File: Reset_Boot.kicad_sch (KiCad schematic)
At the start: 23 parts, among them J301 Micro_SD_Card, J302 Molex PicoBlade 4-pin, Q301 BSS138, SW301 KMR2, SW302 KMR2, U301 SSM2518CPZ

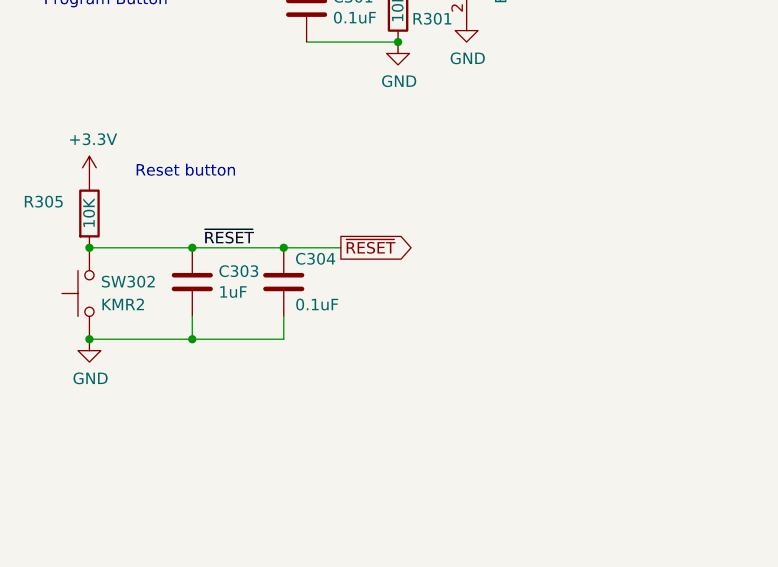
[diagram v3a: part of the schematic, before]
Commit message: Switched to a different 12V booster chip and increased 12V from 500ma to 1A.
Also:
- Switched most 10uF capacitors to 0402 footprints.
- Other cleanup

Signed-off-by: Aaron Williams <aaron.w2@gmail.com>
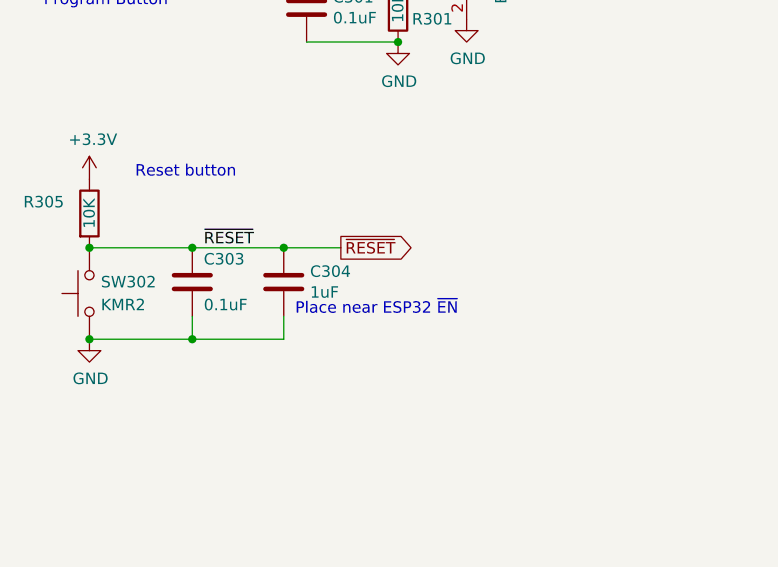
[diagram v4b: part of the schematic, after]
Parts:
- C306: footprint Capacitor_SMD:C_0603_1608Metric -> Capacitor_SMD:C_0402_1005Metric; DESC (none) -> 10 µF ±20% 10V Ceramic Capacitor X5R 0402 (1005 Metric); DK_Datasheet_Link (none) -> https://media.digikey.com/pdf/Data%20Sheets/Samsung%20PDFs/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; DK_Detail_Page (none) -> https://www.digikey.com/en/products/detail/samsung-electro-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; Digi-Key_PN (none) -> 1276-1450-1-ND; MANUFACTURER (none) -> Samsung Electro-Mechanics; MFR (none) -> Samsung Electro-Mechanics; Manufacturer (none) -> Samsung Electro-Mechanics
- renumbered C304 to C303, C303 to C304
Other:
- note added: "Place near ESP32 ~{EN}"
- moved on the sheet: C303, C304
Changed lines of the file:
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@@
   (junction (at 81.28 142.24) (diameter 0) (color 0 0 0 0)
   )
+  (junction (at 48.26 71.12) (diameter 0) (color 0 0 0 0)
+  )
   (junction (at 58.42 71.12) (diameter 0) (color 0 0 0 0)
   )
@@
   (junction (at 248.92 68.58) (diameter 0) (color 0 0 0 0)
   )
-  (junction (at 48.26 71.12) (diameter 0) (color 0 0 0 0)
-  )
   (junction (at 36.83 81.28) (diameter 0) (color 0 0 0 0)
   )
@@
     (stroke (width 0) (type default) (color 0 0 0 0))
   )
+  (wire (pts (xy 48.26 71.12) (xy 58.42 71.12))
+    (stroke (width 0) (type default) (color 0 0 0 0))
+  )
   (wire (pts (xy 92.71 149.86) (xy 81.28 149.86))
     (stroke (width 0) (type default) (color 0 0 0 0))
@@
     (stroke (width 0) (type default) (color 0 0 0 0))
   )
+  (wire (pts (xy 248.92 54.61) (xy 248.92 68.58))
+    (stroke (width 0) (type default) (color 0 0 0 0))
+  )
+  (wire (pts (xy 228.6 68.58) (xy 241.3 68.58))
+    (stroke (width 0) (type default) (color 0 0 0 0))
+  )
+  (wire (pts (xy 182.88 132.08) (xy 196.85 132.08))
+    (stroke (width 0) (type default) (color 0 0 0 0))
+  )
+  (wire (pts (xy 123.19 134.62) (xy 137.16 134.62))
+    (stroke (width 0) (type default) (color 0 0 0 0))
+  )
+  (wire (pts (xy 78.74 35.56) (xy 83.82 35.56))
+    (stroke (width 0) (type default) (color 0 0 0 0))
+  )
+  (wire (pts (xy 248.92 71.12) (xy 248.92 73.66))
+    (stroke (width 0) (type default) (color 0 0 0 0))
+  )
+  (wire (pts (xy 194.31 124.46) (xy 196.85 127))
+    (stroke (width 0) (type default) (color 0 0 0 0))
+  )
+  (wire (pts (xy 196.85 121.92) (xy 203.2 121.92))
+    (stroke (width 0) (type default) (color 0 0 0 0))
+  )
+  (wire (pts (xy 81.28 142.24) (xy 69.85 142.24))
+    (stroke (width 0) (type default) (color 0 0 0 0))
+  )
+  (wire (pts (xy 182.88 55.88) (xy 194.31 55.88))
+    (stroke (width 0) (type default) (color 0 0 0 0))
+  )
+  (wire (pts (xy 137.16 119.38) (xy 137.16 109.22))
+    (stroke (width 0) (type default) (color 0 0 0 0))
+  )
+  (wire (pts (xy 196.85 119.38) (xy 203.2 119.38))
+    (stroke (width 0) (type default) (color 0 0 0 0))
+  )
+  (wire (pts (xy 137.16 124.46) (xy 123.19 124.46))
+    (stroke (width 0) (type default) (color 0 0 0 0))
+  )
+  (wire (pts (xy 228.6 52.07) (xy 241.3 52.07))
+    (stroke (width 0) (type default) (color 0 0 0 0))
+  )
+  (wire (pts (xy 60.96 48.26) (xy 71.12 48.26))
+    (stroke (width 0) (type default) (color 0 0 0 0))
+  )
+  (wire (pts (xy 182.88 127) (xy 194.31 127))
+    (stroke (width 0) (type default) (color 0 0 0 0))
+  )
+  (wire (pts (xy 125.73 149.86) (xy 137.16 149.86))
+    (stroke (width 0) (type default) (color 0 0 0 0))
+  )
   (wire (pts (xy 58.42 71.12) (xy 64.77 71.12))
     (stroke (width 0) (type default) (color 0 0 0 0))
   )
-  (wire (pts (xy 248.92 54.61) (xy 248.92 68.58))
-    (stroke (width 0) (type default) (color 0 0 0 0))
-  )
-  (wire (pts (xy 228.6 68.58) (xy 241.3 68.58))
-    (stroke (width 0) (type default) (color 0 0 0 0))
-  )
-  (wire (pts (xy 182.88 132.08) (xy 196.85 132.08))
-    (stroke (width 0) (type default) (color 0 0 0 0))
-  )
-  (wire (pts (xy 123.19 134.62) (xy 137.16 134.62))
-    (stroke (width 0) (type default) (color 0 0 0 0))
-  )
-  (wire (pts (xy 78.74 35.56) (xy 83.82 35.56))
-    (stroke (width 0) (type default) (color 0 0 0 0))
-  )
-  (wire (pts (xy 248.92 71.12) (xy 248.92 73.66))
-    (stroke (width 0) (type default) (color 0 0 0 0))
-  )
-  (wire (pts (xy 194.31 124.46) (xy 196.85 127))
-    (stroke (width 0) (type default) (color 0 0 0 0))
-  )
-  (wire (pts (xy 196.85 121.92) (xy 203.2 121.92))
-    (stroke (width 0) (type default) (color 0 0 0 0))
-  )
-  (wire (pts (xy 81.28 142.24) (xy 69.85 142.24))
-    (stroke (width 0) (type default) (color 0 0 0 0))
-  )
-  (wire (pts (xy 182.88 55.88) (xy 194.31 55.88))
-    (stroke (width 0) (type default) (color 0 0 0 0))
-  )
-  (wire (pts (xy 137.16 119.38) (xy 137.16 109.22))
-    (stroke (width 0) (type default) (color 0 0 0 0))
-  )
-  (wire (pts (xy 196.85 119.38) (xy 203.2 119.38))
-    (stroke (width 0) (type default) (color 0 0 0 0))
-  )
-  (wire (pts (xy 137.16 124.46) (xy 123.19 124.46))
-    (stroke (width 0) (type default) (color 0 0 0 0))
-  )
-  (wire (pts (xy 228.6 52.07) (xy 241.3 52.07))
-    (stroke (width 0) (type default) (color 0 0 0 0))
-  )
-  (wire (pts (xy 60.96 48.26) (xy 71.12 48.26))
-    (stroke (width 0) (type default) (color 0 0 0 0))
-  )
-  (wire (pts (xy 182.88 127) (xy 194.31 127))
-    (stroke (width 0) (type default) (color 0 0 0 0))
-  )
-  (wire (pts (xy 125.73 149.86) (xy 137.16 149.86))
-    (stroke (width 0) (type default) (color 0 0 0 0))
-  )
   (wire (pts (xy 182.88 119.38) (xy 194.31 119.38))
     (stroke (width 0) (type default) (color 0 0 0 0))
   )
-  (wire (pts (xy 48.26 71.12) (xy 58.42 71.12))
-    (stroke (width 0) (type default) (color 0 0 0 0))
-  )
   (wire (pts (xy 248.92 52.07) (xy 248.92 54.61))
     (stroke (width 0) (type default) (color 0 0 0 0))
@@
   )
   (text "Program Button" (at 31.75 44.45 0)
+    (effects (font (size 1.27 1.27)) (justify left bottom))
+  )
+  (text "Place near ESP32 ~{EN}" (at 59.69 78.74 0)
     (effects (font (size 1.27 1.27)) (justify left bottom))
   )
@@
     (pin "1")
   )
-  (symbol (lib_id "Device:C") (at 48.26 74.93 0) (unit 1)
-    (in_bom yes) (on_board yes)
-    (property "Reference" "C303" (id 0) (at 51.181 73.7616 0)
-      (effects (font (size 1.27 1.27)) (justify left))
-    )
-    (property "Value" "1uF" (id 1) (at 51.181 76.073 0)
-      (effects (font (size 1.27 1.27)) (justify left))
-    )
-    (property "Footprint" "Capacitor_SMD:C_0402_1005Metric" (id 2) (at 49.2252 78.74 0)
-      (effects (font (size 1.27 1.27)) hide)
-    )
-    (property "Datasheet" "~" (id 3) (at 48.26 74.93 0)
-      (effects (font (size 1.27 1.27)) hide)
-    )
-    (property "DESC" "" (id 9) (at -49.53 172.72 0)
+  (symbol (lib_id "Device:C") (at 58.42 74.93 0) (unit 1)
+    (in_bom yes) (on_board yes)
+    (property "Reference" "C304" (id 0) (at 61.341 73.7616 0)
+      (effects (font (size 1.27 1.27)) (justify left))
+    )
+    (property "Value" "1uF" (id 1) (at 61.341 76.073 0)
+      (effects (font (size 1.27 1.27)) (justify left))
+    )
+    (property "Footprint" "Capacitor_SMD:C_0402_1005Metric" (id 2) (at 59.3852 78.74 0)
+      (effects (font (size 1.27 1.27)) hide)
+    )
+    (property "Datasheet" "~" (id 3) (at 58.42 74.93 0)
+      (effects (font (size 1.27 1.27)) hide)
+    )
+    (property "DESC" "" (id 9) (at -39.37 172.72 0)
       (effects (font (size 1.27 1.27)) hide)
     )
@@
       (effects (font (size 1.27 1.27)) (justify left))
     )
-    (property "Footprint" "Capacitor_SMD:C_0603_1608Metric" (id 2) (at 82.2452 149.86 0)
+    (property "Footprint" "Capacitor_SMD:C_0402_1005Metric" (id 2) (at 82.2452 149.86 0)
       (effects (font (size 1.27 1.27)) hide)
     )
@@
       (effects (font (size 1.27 1.27)) hide)
     )
-    (property "MFR" "" (id 4) (at -31.75 213.36 0)
+    (property "MFR" "Samsung Electro-Mechanics" (id 4) (at -31.75 213.36 0)
       (effects (font (size 1.27 1.27)) hide)
     )
@@
       (effects (font (size 1.27 1.27)) hide)
     )
-    (property "DESC" "" (id 9) (at -31.75 213.36 0)
+    (property "DESC" "10 µF ±20% 10V Ceramic Capacitor X5R 0402 (1005 Metric)" (id 9) (at -31.75 213.36 0)
+      (effects (font (size 1.27 1.27)) hide)
+    )
+    (property "DK_Datasheet_Link" "https://media.digikey.com/pdf/Data%20Sheets/Samsung%20PDFs/CL05A106MP5NUNC_Spec.pdf" (id 10) (at 81.28 146.05 0)
+      (effects (font (size 1.27 1.27)) hide)
+    )
+    (property "DK_Detail_Page" "https://www.digikey.com/en/products/detail/samsung-electro-mechanics/CL05A106MP5NUNC/3887108" (id 11) (at 81.28 146.05 0)
+      (effects (font (size 1.27 1.27)) hide)
+    )
+    (property "Digi-Key_PN" "1276-1450-1-ND" (id 12) (at 81.28 146.05 0)
+      (effects (font (size 1.27 1.27)) hide)
+    )
+    (property "MANUFACTURER" "Samsung Electro-Mechanics" (id 13) (at 81.28 146.05 0)
+      (effects (font (size 1.27 1.27)) hide)
+    )
+    (property "Manufacturer" "Samsung Electro-Mechanics" (id 14) (at 81.28 146.05 0)
       (effects (font (size 1.27 1.27)) hide)
     )
@@
     (pin "2")
   )
-  (symbol (lib_id "Device:C") (at 58.42 74.93 0) (unit 1)
-    (in_bom yes) (on_board yes)
-    (property "Reference" "C304" (id 0) (at 59.69 72.39 0)
-      (effects (font (size 1.27 1.27)) (justify left))
-    )
-    (property "Value" "0.1uF" (id 1) (at 59.69 77.47 0)
-      (effects (font (size 1.27 1.27)) (justify left))
-    )
-    (property "Footprint" "Capacitor_SMD:C_0402_1005Metric" (id 2) (at 59.3852 78.74 0)
-      (effects (font (size 1.27 1.27)) hide)
-    )
-    (property "Datasheet" "~" (id 3) (at 58.42 74.93 0)
-      (effects (font (size 1.27 1.27)) hide)
-    )
-    (property "SPR" "Digikey" (id 6) (at 58.42 74.93 0)
-      (effects (font (size 1.27 1.27)) hide)
-    )
-    (property "DESC" "" (id 9) (at -27.94 140.97 0)
-      (effects (font (size 1.27 1.27)) hide)
-    )
+  (symbol (lib_id "Device:C") (at 48.26 74.93 0) (unit 1)
+    (in_bom yes) (on_board yes)
+    (property "Reference" "C303" (id 0) (at 49.53 72.39 0)
+      (effects (font (size 1.27 1.27)) (justify left))
+    )
+    (property "Value" "0.1uF" (id 1) (at 49.53 77.47 0)
+      (effects (font (size 1.27 1.27)) (justify left))
+    )
+    (property "Footprint" "Capacitor_SMD:C_0402_1005Metric" (id 2) (at 49.2252 78.74 0)
+      (effects (font (size 1.27 1.27)) hide)
+    )
+    (property "Datasheet" "~" (id 3) (at 48.26 74.93 0)
+      (effects (font (size 1.27 1.27)) hide)
+    )
+    (property "SPR" "Digikey" (id 6) (at 48.26 74.93 0)
+      (effects (font (size 1.27 1.27)) hide)
+    )
+    (property "DESC" "" (id 9) (at -38.1 140.97 0)
+      (effects (font (size 1.27 1.27)) hide)
+    )

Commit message: Latest 4.0 settings for pcbway
Signed-off-by: Aaron Williams <aaron.w2@gmail.com>
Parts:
- added TP301: ~{RESET}, TestPoint:TestPoint_Pad_1.0x1.0mm, symbol Connector:TestPoint
- C302: DESC (none) -> CAP CER 1UF 25V X5R 0402; Digi-Key_PN (none) -> 490-GRM155R61E105MA12JCT-ND; MANUFACTURER (none) -> Murata Electronics; MFR (none) -> Murata Electronics; MPN (none) -> GRM155R61E105MA12J; Manufacturer (none) -> Murata Electronics; Manufacturer Part Number (none) -> GRM155R61E105MA12J; SPN (none) -> 490-GRM155R61E105MA12JCT-ND; SPURL (none) -> https://www.digikey.com/en/products/detail/murata-electroni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
- C304: DESC (none) -> CAP CER 1UF 25V X5R 0402; Digi-Key_PN (none) -> 490-GRM155R61E105MA12JCT-ND; MANUFACTURER (none) -> Murata Electronics; MFR (none) -> Murata Electronics; MPN (none) -> GRM155R61E105MA12J; Manufacturer (none) -> Murata Electronics; Manufacturer Part Number (none) -> GRM155R61E105MA12J; SPN (none) -> 490-GRM155R61E105MA12JCT-ND; SPR (none) -> Digikey; SPURL (none) -> https://www.digikey.com/en/products/detail/murata-electroni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
- J301: DK_Datasheet_Link (none) -> https://media.digikey.com/pdf/Data%20Sheets/Molex%20PDFs/04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; DK_Detail_Page (none) -> https://www.digikey.com/en/products/detail/molex/0475710001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; MANUFACTURER (none) -> Molex; Manufacturer (none) -> Molex; Manufacturer Part Number (none) -> 0475710001
- J302: DESC (none) -> Connector Header Through Hole 4 position 0.049" (1.25mm); MANUFACTURER (none) -> Molex; MFR (none) -> Molex; MPN (none) -> 0530470460; Manufacturer (none) -> Molex; Manufacturer Part Number (none) -> 0530470460; SPN (none) -> 900-0530470460-ND; SPR (none) -> Digikey; SPURL (none) -> https://www.digikey.com/en/products/detail/molex/0530470460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
- R301, R302, R303, R304, R305, R306, R307, R308, R309: DESC (none) -> 10 kOhms ±1% 0.063W, 1/16W Chip Resistor 0402 (1005 Metric)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; Digi-Key_PN (none) -> 311-10.0KLRCT-ND; MANUFACTURER (none) -> YAGEO; MFR (none) -> YAGEO; MPN (none) -> RC0402FR-0710KL; Manufacturer (none) -> YAGEO; Manufacturer Part Number (none) -> RC0402FR-0710KL; SPN 541-2979-1-ND -> 311-10.0KLRCT-ND; SPURL https://www.digikey.com/products/en?keywords=541-2979-1-ND -> https://www.digikey.com/en/products/detail/yageo/RC0402FR-0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; Tolerance 5% -> (none)
- U301: MFR (none) -> Analog Devices Inc.; MPN (none) -> SSM2518CPZ; SPN (none) -> 505-SSM2518CPZ-ND; SPR (none) -> Digikey; SPURL (none) -> https://www.digikey.com/en/products/detail/analog-devices-i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
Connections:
- net +3V3: no longer U301.3 (ADDR)
- net GND: now also U301.3 (ADDR)
- net ~{RESET}: now also TP301.1
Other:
- note added: "I2C address 0x34"
- moved on the sheet: C308, Q301, R309

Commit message: Minor fixes.
Signed-off-by: Aaron Williams <aaron.w2@gmail.com>
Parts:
- Q301: value BSS138 -> BSS138PW,115; DESC N-Channel 50V 220mA (Ta) 360mW (Ta) Surface Mount SOT-23-3 -> N-Channel 60 V 320mA (Ta) 260mW (Ta), 830mW (Tc) Surface Mo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; DK_Detail_Page (none) -> https://www.digikey.com/en/products/detail/nexperia-usa-inc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; Digi-Key_PN (none) -> 1727-1143-1-ND; MANUFACTURER (none) -> Nexperia USA Inc.; MFR ON Semiconductor -> Nexperia USA Inc.; MPN BSS138 -> BSS138PW,115; Manufacturer (none) -> Nexperia USA Inc.; Manufacturer Part Number (none) -> BSS138PW,115; SPN BSS138CT-ND -> 1727-1143-1-ND; SPURL https://www.digikey.com/product-detail/en/on-semiconductor/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 -> https://www.digikey.com/en/products/detail/nexperia-usa-inc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
- TP301: now left out of the parts list
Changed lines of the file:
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@@
     (in_bom yes) (on_board yes)
     (property "Reference" "Q301" (id 0) (at 87.4268 40.64 90))
-    (property "Value" "BSS138" (id 1) (at 85.1154 40.64 90))
+    (property "Value" "BSS138PW,115" (id 1) (at 85.09 43.18 90))
     (property "Footprint" "Package_TO_SOT_SMD:SOT-323_SC-70" (id 2) (at 83.82 42.545 0)
       (effects (font (size 1.27 1.27) italic) (justify left) hide)
     )
-    (property "Datasheet" "https://www.onsemi.com/pub/Collateral/BSS138-D.PDF" (id 3) (at 78.74 40.64 0)
+    (property "Datasheet" "https://assets.nexperia.com/documents/data-sheet/BSS138PW.pdf" (id 3) (at 78.74 40.64 0)
       (effects (font (size 1.27 1.27)) (justify left) hide)
     )
-    (property "MFR" "ON Semiconductor" (id 4) (at 78.74 40.64 0)
-      (effects (font (size 1.27 1.27)) hide)
-    )
-    (property "MPN" "BSS138" (id 5) (at 78.74 40.64 0)
+    (property "MFR" "Nexperia USA Inc." (id 4) (at 78.74 40.64 0)
+      (effects (font (size 1.27 1.27)) hide)
+    )
+    (property "MPN" "BSS138PW,115" (id 5) (at 78.74 40.64 0)
       (effects (font (size 1.27 1.27)) hide)
     )
@@
       (effects (font (size 1.27 1.27)) hide)
     )
-    (property "SPN" "BSS138CT-ND" (id 7) (at 78.74 40.64 0)
-      (effects (font (size 1.27 1.27)) hide)
-    )
-    (property "SPURL" "https://www.digikey.com/product-detail/en/on-semiconductor/BSS138/BSS138CT-ND/244294" (id 8) (at 78.74 40.64 0)
-      (effects (font (size 1.27 1.27)) hide)
-    )
-    (property "DESC" "N-Channel 50V 220mA (Ta) 360mW (Ta) Surface Mount SOT-23-3" (id 9) (at -52.07 102.87 0)
+    (property "SPN" "1727-1143-1-ND" (id 7) (at 78.74 40.64 0)
+      (effects (font (size 1.27 1.27)) hide)
+    )
+    (property "SPURL" "https://www.digikey.com/en/products/detail/nexperia-usa-inc/BSS138PW-115/2779826" (id 8) (at 78.74 40.64 0)
+      (effects (font (size 1.27 1.27)) hide)
+    )
+    (property "DESC" "N-Channel 60 V 320mA (Ta) 260mW (Ta), 830mW (Tc) Surface Mount SOT-323" (id 9) (at -52.07 102.87 0)
+      (effects (font (size 1.27 1.27)) hide)
+    )
+    (property "DK_Detail_Page" "https://www.digikey.com/en/products/detail/nexperia-usa-inc/BSS138PW-115/2779826" (id 10) (at 78.74 40.64 0)
+      (effects (font (size 1.27 1.27)) hide)
+    )
+    (property "Description" "MOSFET N-CH 60V 320MA SOT323" (id 11) (at 78.74 40.64 0)
+      (effects (font (size 1.27 1.27)) hide)
+    )
+    (property "Digi-Key_PN" "1727-1143-1-ND" (id 12) (at 78.74 40.64 0)
+      (effects (font (size 1.27 1.27)) hide)
+    )
+    (property "MANUFACTURER" "Nexperia USA Inc." (id 13) (at 78.74 40.64 0)
+      (effects (font (size 1.27 1.27)) hide)
+    )
+    (property "Manufacturer" "Nexperia USA Inc." (id 14) (at 78.74 40.64 0)
+      (effects (font (size 1.27 1.27)) hide)
+    )
+    (property "Manufacturer Part Number" "BSS138PW,115" (id 15) (at 78.74 40.64 0)
       (effects (font (size 1.27 1.27)) hide)
     )
@@
   )
   (symbol (lib_id "Connector:TestPoint") (at 58.42 67.31 0) (unit 1)
-    (in_bom yes) (on_board yes) (fields_autoplaced)
+    (in_bom no) (on_board yes) (fields_autoplaced)
     (property "Reference" "TP301" (id 0) (at 60.96 62.7379 0)
       (effects (font (size 1.27 1.27)) (justify left))
